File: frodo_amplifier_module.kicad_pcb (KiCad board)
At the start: 4 copper layers, 24.5 x 12.5 mm, 37 parts, among them IC1 INA826AID, J1 JST-GH, J2 JST-GH, J3 JST-GH, J4 JST-GH, U1 ADC101C021CIMK, U2 MCP6001-OT, U3 MIC5504-3.3YM5, U4 REF3033

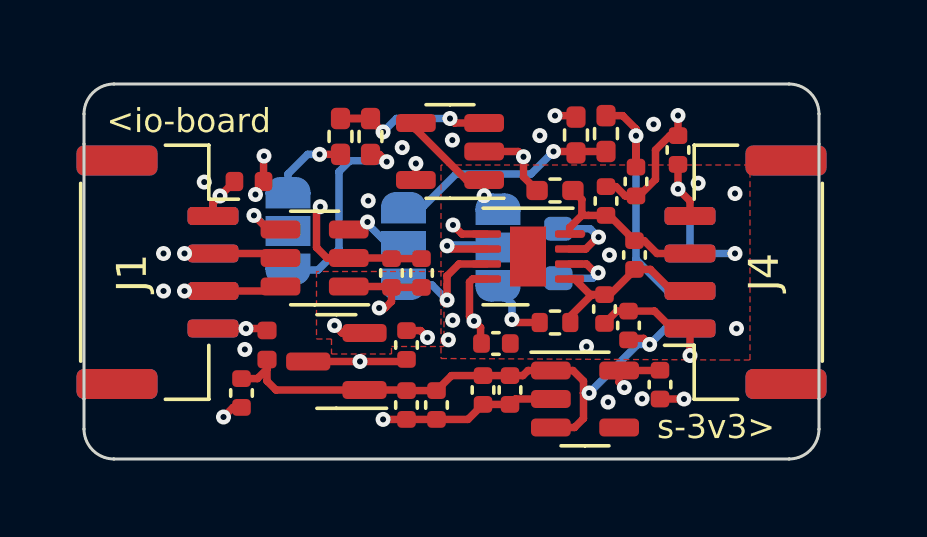
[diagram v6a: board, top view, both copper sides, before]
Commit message: remove 3v3ref, merge fills, adjust layout, fill BOM
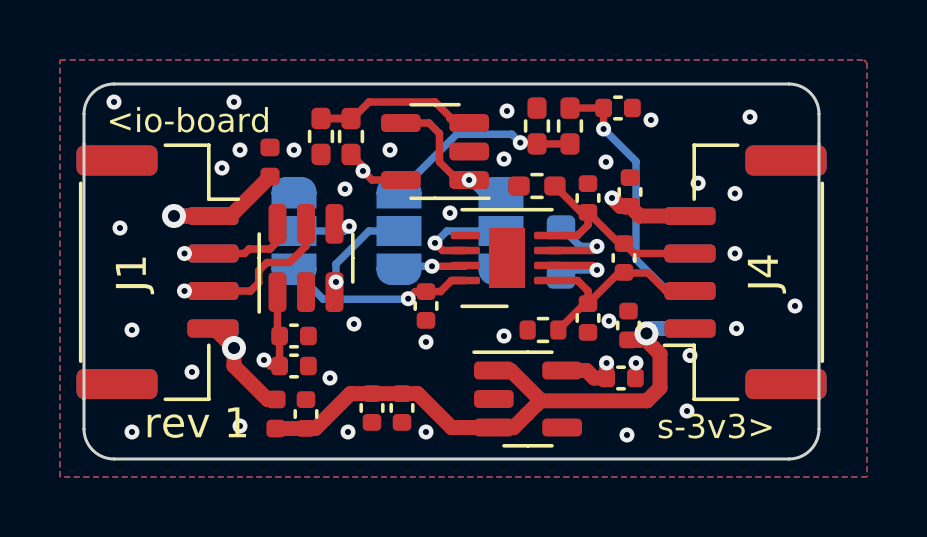
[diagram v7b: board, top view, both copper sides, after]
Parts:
- removed C11: 470n, Capacitor_SMD:C_0402_1005Metric
- removed C12, C13: 0u1, Capacitor_SMD:C_0402_1005Metric
- removed U4: REF3033, Package_TO_SOT_SMD:SOT-23
- C14, C3: value 0u1 -> 100n
- moved C2 5.26 mm to (58.0, 43.4), turned to 0 degrees
- moved C3 3.87 mm to (58.0, 42.4), turned to 0 degrees
- moved C15 3.75 mm to (60.6, 44.8)
- moved C14 3.65 mm to (61.6, 44.8)
- moved C4 2.64 mm to (62.4, 41.4), turned to -90 degrees
- moved C6 2.52 mm to (68.8, 34.8), turned to 0 degrees
- moved FB1 2.32 mm to (57.4, 45.0)
- moved C1 2.26 mm to (58.4, 45.0), turned to 90 degrees
- moved C8 2.13 mm to (69.2, 37.6)
- moved U3 1.90 mm to (65.8, 44.5)
- moved R4 1.33 mm to (66.1, 35.4)
- moved C16 1.32 mm to (68.9, 43.8), turned to 0 degrees
- moved R3 1.23 mm to (67.2, 35.4)
- moved FB2 0.96 mm to (57.2, 36.6), turned to 90 degrees
- moved IC1 0.70 mm to (65.1, 39.8)
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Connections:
- C2 pad 1: 3V3Ref -> 3V3
- C3 pad 1: 3V3Ref -> 3V3
- J1 pad 2: SCL -> SDA
- J1 pad 3: SDA -> SCL
- J2 pad 2: SDA -> SCL
- J2 pad 3: SCL -> SDA
- U1 pad 1: 3V3Ref -> 3V3
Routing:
- net GND: track 37.9 -> 0.12 mm, vias 33 -> 34
- net 3V3Ref: track 5.31 -> 0.00 mm, vias 3 -> 0
- net Net-(J1-Pin_1): track 2.76 -> 5.59 mm
- net 3V3: track 14.3 -> 16.5 mm
- net sig: track 3.94 -> 2.27 mm
- net SCL: track 4.21 -> 5.64 mm
- net Net-(J1-Pin_4): track 3.08 -> 4.40 mm
- net +IN: track 6.27 -> 7.31 mm
- net Net-(J3-Pin_3): track 9.86 -> 8.85 mm
- net sig2: track 7.52 -> 6.63 mm
- net -IN: track 6.54 -> 7.32 mm
- net Net-(JP1-C): track 2.45 -> 3.16 mm
- net Net-(JP3-B): track 4.27 -> 4.85 mm
- net Net-(IC1-RG_2): track 2.58 -> 3.13 mm
- net Net-(U2-+): track 6.22 -> 6.49 mm, vias 2 -> 0
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- added copper zone on B.Cu, net GND
- removed copper zone on F.Cu, net 3V3Ref
- removed copper zone on In2.Cu, net 3V3Ref
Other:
- board text added: "JLCJLCJLCJLC"
- board text added: "rev 1"

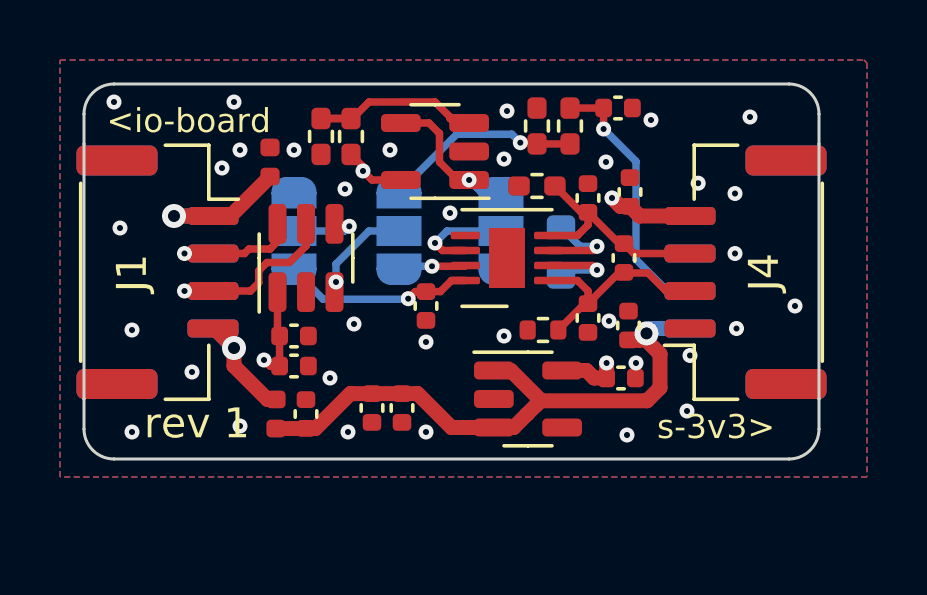
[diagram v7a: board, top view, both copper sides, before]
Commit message: finished amp module rev3
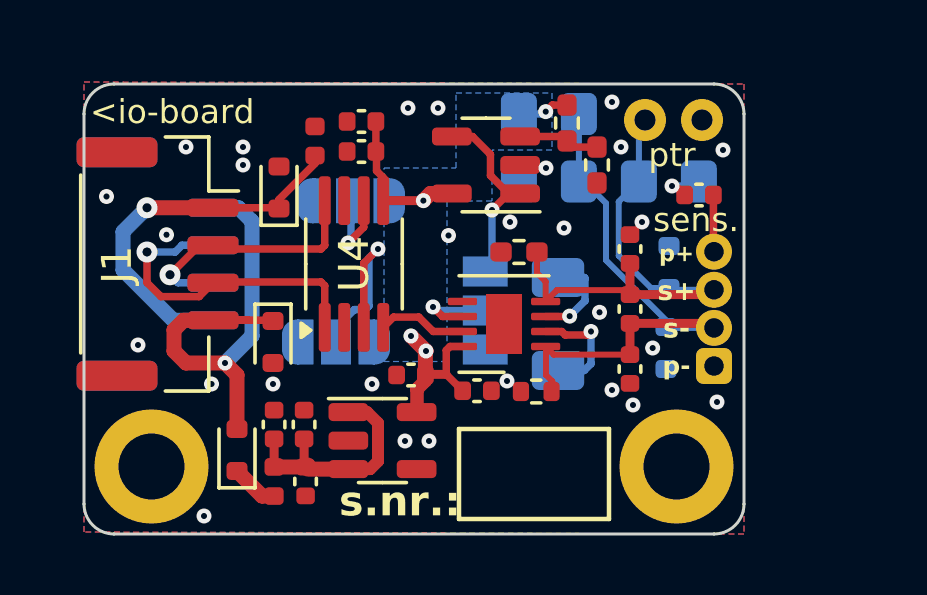
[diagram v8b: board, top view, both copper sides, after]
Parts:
- removed C5: 10n, Capacitor_SMD:C_0402_1005Metric
- removed C6: 2n2, Capacitor_SMD:C_0402_1005Metric
- removed J4: JST-GH, Connector_JST:JST_GH_SM04B-GHS-TB_1x04-1MP_P1.25mm_Horizontal
- removed R4: 10k, Resistor_SMD:R_0402_1005Metric_Pad0.72x0.64mm_HandSolder
- removed U1: ADC101C021CIMK, Package_TO_SOT_SMD:SOT-23-6
- added D1: 1N4148WT, Diode_SMD:D_SOD-523, F.Cu at (56.1, 46.2)
- added D2: ESD5Zxx, Diode_SMD:D_SOD-523, B.Cu at (70.4, 42.8)
- added D3: ESD5Zxx, Diode_SMD:D_SOD-523, B.Cu at (70.5, 40.1)
- added D4: ESD5Zxx, Diode_SMD:D_SOD-523, F.Cu at (57.3, 42.6)
- added D5: ESD5Zxx, Diode_SMD:D_SOD-523, F.Cu at (57.5, 37.5)
- added H1: MountingHole, MountingHole:MountingHole_2.2mm_M2_DIN965_Pad, F.Cu at (70.8, 46.8)
- added H2: MountingHole, MountingHole:MountingHole_2.2mm_M2_DIN965_Pad, F.Cu at (53.2, 46.8)
- added J5: Conn_01x04_Socket, Connector_PinHeader_1.27mm:PinHeader_1x04_P1.27mm_Vertical, F.Cu at (72.0, 43.4)
- added R7: R100/1k, Resistor_SMD:R_0805_2012Metric_Pad1.20x1.40mm_HandSolder, B.Cu at (66.5, 37.2)
- added R8: R100/1k, Resistor_SMD:R_0805_2012Metric_Pad1.20x1.40mm_HandSolder, B.Cu at (66.5, 35.0)
- added U4: ADC101C021CIMM, Package_SO:MSOP-8_3x3mm_P0.65mm, F.Cu at (60.0, 40.0)
- J3: value JST-GH -> Conn_01x02_Socket; footprint Connector_JST:JST_GH_SM04B-GHS-TB_1x04-1MP_P1.25mm_Horizontal -> Resistor_THT:R_Axial_DIN0204_L3.6mm_D1.6mm_P1.90mm_Vertical; moved to F.Cu
- JP3: footprint Jumper:SolderJumper-3_P1.3mm_Open_RoundedPad1.0x1.5mm_NumberLabels -> Jumper:SolderJumper-3_P1.3mm_Open_Pad1.0x1.5mm
- R3: value 5k -> R100/1k; footprint Resistor_SMD:R_0402_1005Metric_Pad0.72x0.64mm_HandSolder -> Resistor_SMD:R_0805_2012Metric_Pad1.20x1.40mm_HandSolder; moved to B.Cu
- RG1: footprint Resistor_SMD:R_0603_1608Metric -> Resistor_SMD:R_1206_3216Metric_Pad1.30x1.75mm_HandSolder
- moved R6 9.25 mm to (68.1, 36.7)
- moved C2 8.45 mm to (60.2, 35.2), turned to 180 degrees
- moved R5 7.21 mm to (67.1, 35.3), turned to 90 degrees
- moved C16 7.00 mm to (61.9, 43.7), turned to 180 degrees
- moved C3 6.55 mm to (60.2, 36.2), turned to 180 degrees
- moved J3 6.08 mm to (69.7, 35.2), turned to 0 degrees
- moved U3 5.05 mm to (60.9, 45.9)
- moved JP2 3.96 mm to (59.4, 42.6), turned to 0 degrees
- moved R3 3.78 mm to (70.5, 37.2), turned to 0 degrees
- moved C14 3.31 mm to (58.3, 45.4), turned to 90 degrees
- moved C15 3.30 mm to (58.4, 47.2)
- moved C4 3.30 mm to (64.1, 44.2), turned to 0 degrees
- moved JP3 2.70 mm to (64.4, 41.5)
- moved RG1 2.40 mm to (66.8, 42.0)
- moved C8 2.30 mm to (71.5, 37.7), turned to 180 degrees
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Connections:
- net -IN renamed s-
- C7 pad 1: +IN -> s+
- C9 pad 1: +IN -> s+
- FB1 pad 1: Net-(J1-Pin_4) -> Net-(D1-K)
- FB2 pad 1: Net-(J1-Pin_1) -> Net-(D5-K)
- IC1 pad 4: +IN -> s+
- J1 pad 1: Net-(J1-Pin_1) -> Net-(D5-K)
- J1 pad 4: Net-(J1-Pin_4) -> Net-(D1-A)
- J1 pad MP: unconnected-(J1-MountPin-PadMP) -> GND
- J2 pad 1: Net-(J1-Pin_4) -> Net-(D5-K)
- J2 pad 2: SCL -> SDA
- J2 pad 3: SDA -> SCL
- J2 pad 4: Net-(J1-Pin_1) -> Net-(D1-A)
- J2 pad MP: unconnected-(J2-MountPin-PadMP) -> GND
- J3 pad 1: GND -> s+
- J3 pad 2: GND -> 3V3
- JP1 pad 1: sig2 -> GND
- JP1 pad 3: sig -> 3V3
- R2 pad 2: +IN -> s+
- R3 pad 1: sig2 -> s+
- R3 pad 2: Net-(J3-Pin_3) -> GND
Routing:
- net s+: track 0.00 -> 17.2 mm
- net Net-(D1-A): track 0.00 -> 16.2 mm, vias 0 -> 1
- net 5V: track 20.9 -> 8.01 mm, vias 1 -> 0
- net Net-(D5-K): track 0.00 -> 12.8 mm, vias 0 -> 1
- net s-: track 7.32 -> 18.5 mm
- net Net-(J3-Pin_3): track 8.85 -> 0.00 mm, vias 1 -> 0
- net +IN: track 7.31 -> 0.00 mm
- net sig2: track 6.63 -> 0.00 mm, vias 1 -> 0
- net Net-(J1-Pin_1): track 5.59 -> 0.00 mm, vias 1 -> 0
- net SCL: track 5.64 -> 11.1 mm
- net SDA: track 3.85 -> 8.70 mm
- net Net-(J1-Pin_4): track 4.40 -> 0.00 mm, vias 1 -> 0
- net Net-(JP2-C): track 2.44 -> 6.70 mm
- net Net-(U2-+): track 6.49 -> 2.71 mm
- net 3V3: track 16.5 -> 14.5 mm, vias 5 -> 4
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- added copper zone on B.Cu, net 3V3
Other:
- board size 24.5 x 12.5 mm -> 22 x 15 mm
- board text added: "ptr"
- board text added: "rapid amp-board v2"
- board text added: "ref"
- board text added: "s.nr.:"
- board text added: "sens."
- board text removed: "<s-5v"
- board text removed: "JLCJLCJLCJLC"
- board text removed: "rev 1"
- board text removed: "s-3v3>"
